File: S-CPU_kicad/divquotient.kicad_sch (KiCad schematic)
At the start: 97 parts

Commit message: Schematics update.
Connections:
- net OAGE: no longer FGKE.1, HIPM.1, KBGM.3 (CLK), KBGM.4 (~{CLK})
- new net wOAGE_SYSCLK: FGKE.1, HIPM.1, KBGM.3 (CLK), KBGM.4 (~{CLK})
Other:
- company: Regis Galland -> Author: Regis Galland
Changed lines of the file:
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@@
     (date "2023-06-14")
     (rev "0.1")
-    (company "Regis Galland")
+    (company "Author: Regis Galland")
   )
   (junction (at 346.71 195.58) (diameter 0) (color 0 0 0 0)
@@
     (stroke (width 0) (type default))
   )
-  (wire (pts (xy 546.735 464.82) (xy 539.115 464.82))
+  (wire (pts (xy 546.735 464.82) (xy 529.59 464.82))
     (stroke (width 0) (type default))
   )
@@
     (stroke (width 0) (type default))
   )
+  (wire (pts (xy 511.175 398.145) (xy 526.415 398.145))
+    (stroke (width 0) (type default))
+  )
   (wire (pts (xy 379.73 137.16) (xy 379.73 111.125))
     (stroke (width 0) (type default))
@@
   )
   (wire (pts (xy 341.63 511.175) (xy 341.63 494.665))
-    (stroke (width 0) (type default))
-  )
-  (wire (pts (xy 516.255 398.145) (xy 526.415 398.145))
     (stroke (width 0) (type default))
   )
@@
     (effects (font (size 1.27 1.27)) (justify right bottom))
   )
-  (label "OAGE" (at 516.255 398.145 0) (fields_autoplaced)
+  (label "wOAGE_SYSCLK" (at 511.175 398.145 0) (fields_autoplaced)
     (effects (font (size 1.27 1.27)) (justify left bottom))
   )
@@
     (effects (font (size 1.27 1.27)) (justify left bottom))
   )
-  (label "OAGE" (at 539.115 464.82 0) (fields_autoplaced)
+  (label "wOAGE_SYSCLK" (at 529.59 464.82 0) (fields_autoplaced)
     (effects (font (size 1.27 1.27)) (justify left bottom))
   )
@@
     (effects (font (size 1.27 1.27)) (justify left))
   )
-  (hierarchical_label "OAGE" (shape input) (at 516.255 398.145 180) (fields_autoplaced)
+  (hierarchical_label "wOAGE_SYSCLK" (shape input) (at 511.175 398.145 180) (fields_autoplaced)
     (effects (font (size 1.27 1.27)) (justify right))
   )

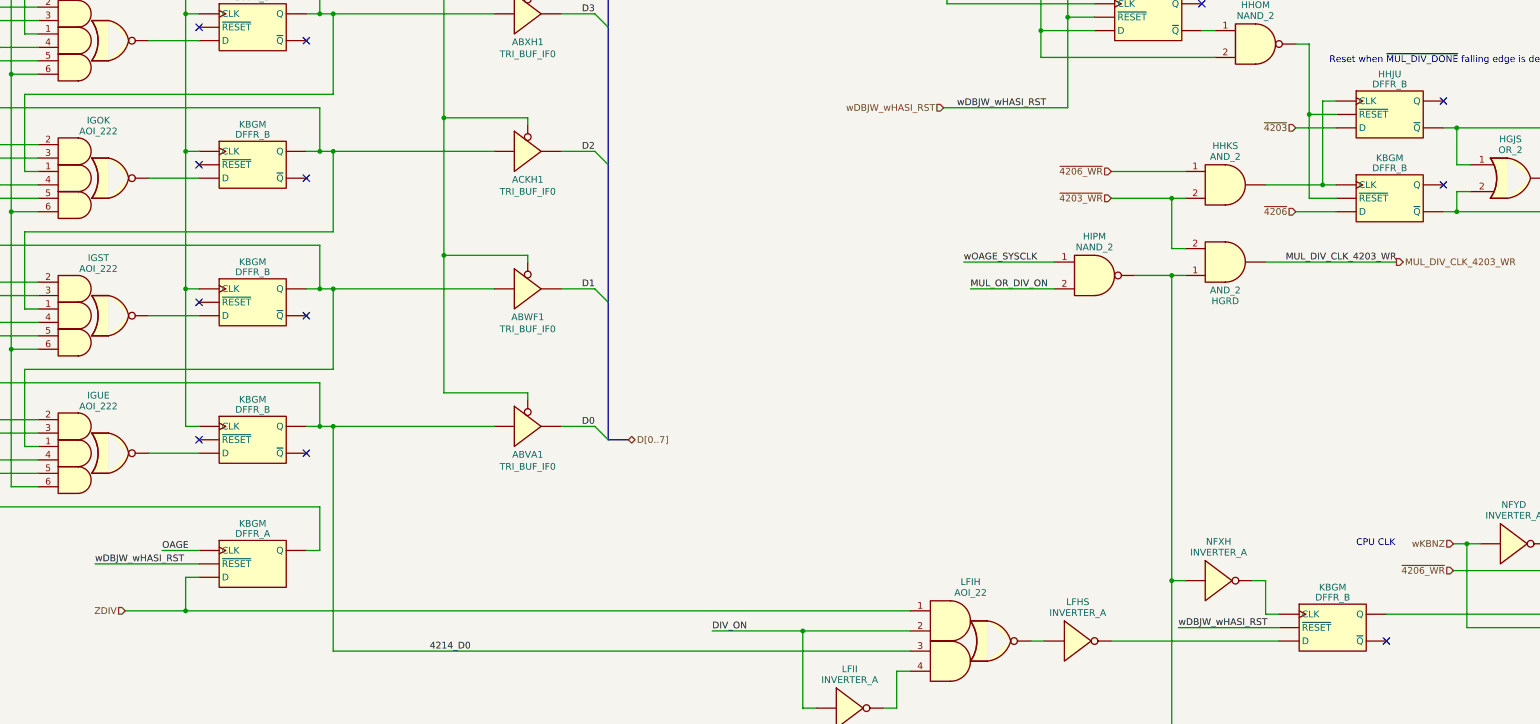
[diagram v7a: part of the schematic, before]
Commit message: Schematics tidying in progress.
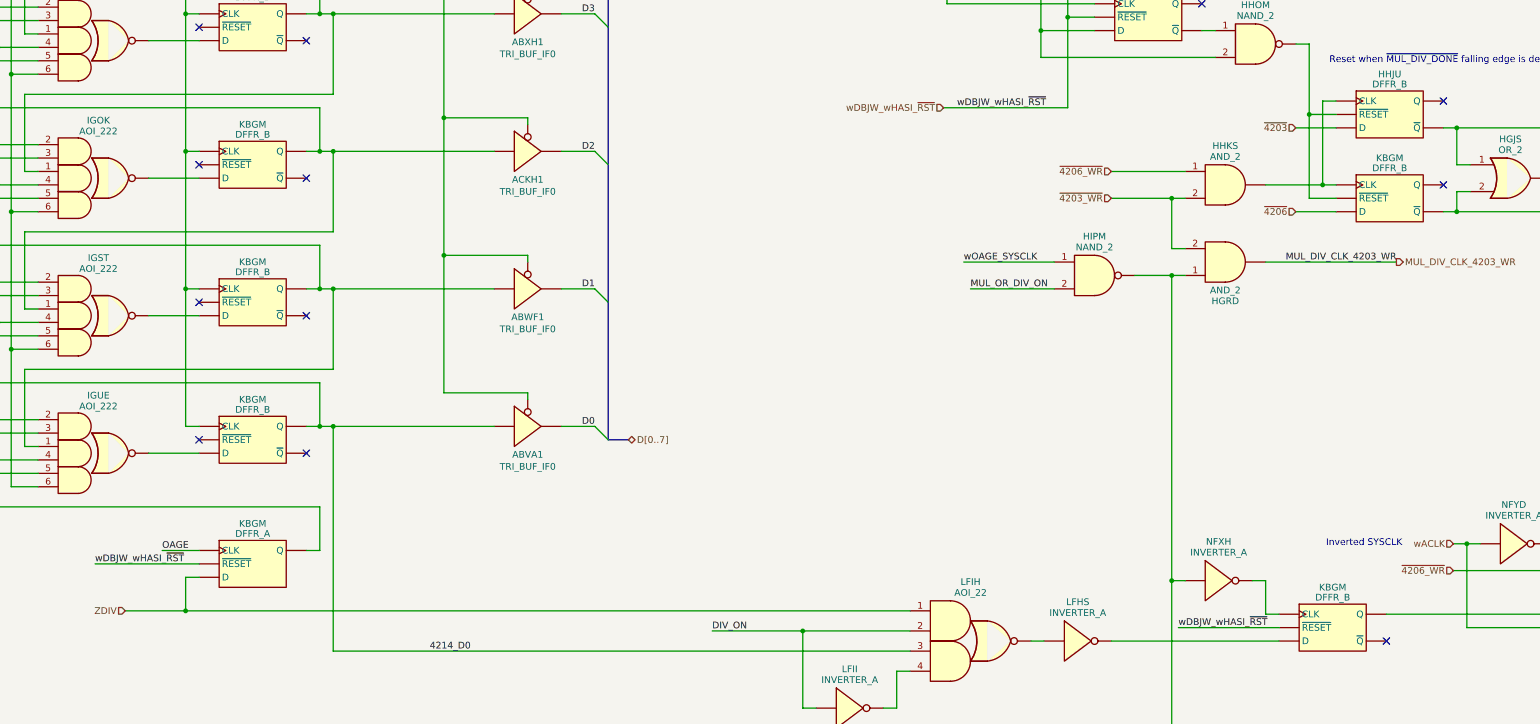
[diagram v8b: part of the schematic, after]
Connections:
- net wDBJW_wHASI_RST renamed wDBJW_wHASI_~{RST}
- net wKBNZ renamed wACLK
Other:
- note added: "Inverted SYSCLK"
- note removed: "CPU CLK"
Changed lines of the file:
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@@
   (title_block
     (title "SNES S-CPU Schematics ")
-    (date "2023-06-14")
+    (date "2023-10-19")
     (rev "0.1")
     (company "Author: Regis Galland")
@@
     (effects (font (size 5 5) (thickness 1) bold) (justify left bottom))
   )
-  (text "CPU CLK" (at 603.885 518.795 0)
+  (text "Inverted SYSCLK" (at 598.17 518.795 0)
     (effects (font (size 1.27 1.27)) (justify left bottom))
   )
@@
     (effects (font (size 1.27 1.27)) (justify left bottom))
   )
-  (label "wDBJW_wHASI_RST" (at 528.32 435.61 0) (fields_autoplaced)
-    (effects (font (size 1.27 1.27)) (justify left bottom))
-  )
-  (label "wDBJW_wHASI_RST" (at 365.125 521.97 0) (fields_autoplaced)
+  (label "wDBJW_wHASI_~{RST}" (at 528.32 435.61 0) (fields_autoplaced)
+    (effects (font (size 1.27 1.27)) (justify left bottom))
+  )
+  (label "wDBJW_wHASI_~{RST}" (at 365.125 521.97 0) (fields_autoplaced)
     (effects (font (size 1.27 1.27)) (justify left bottom))
   )
@@
     (effects (font (size 1.27 1.27)) (justify left bottom))
   )
-  (label "wDBJW_wHASI_RST" (at 570.23 534.035 0) (fields_autoplaced)
+  (label "wDBJW_wHASI_~{RST}" (at 570.23 534.035 0) (fields_autoplaced)
     (effects (font (size 1.27 1.27)) (justify left bottom))
   )
@@
     (effects (font (size 1.27 1.27)) (justify right))
   )
-  (hierarchical_label "wDBJW_wHASI_RST" (shape input) (at 525.78 435.61 180) (fields_autoplaced)
+  (hierarchical_label "wDBJW_wHASI_~{RST}" (shape input) (at 525.78 435.61 180) (fields_autoplaced)
     (effects (font (size 1.27 1.27)) (justify right))
   )
@@
     (effects (font (size 1.27 1.27)) (justify left))
   )
-  (hierarchical_label "wKBNZ" (shape input) (at 622.3 518.16 180) (fields_autoplaced)
+  (hierarchical_label "wACLK" (shape input) (at 622.3 518.16 180) (fields_autoplaced)
     (effects (font (size 1.27 1.27)) (justify right))
   )
